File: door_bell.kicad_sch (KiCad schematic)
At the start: 76 parts, among them J1 8-10V AC/DC, J2 Speaker, J3 SWITCH1, J4 SWITCH2, J5 UART, J6 JTAG, J7 BOOT, J8 MicroSD, J9 Door panel, K1 HJR 1-2C, Q1 BC338, SW1 Reset, U1 NCP1117-5v, U2 MAX98357A, U3 NCP1117-3v3, U4 DS3231M, U5 MAX3232, U6 ESP32-WROVER-B, U7 74LVC2G14

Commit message: Update annotations
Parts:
- renumbered D9 to D10, D10 to D11, D11 to D3, D3 to D4, D4 to D5, D5 to D8, D8 to D9, R7 to R10, R10 to R11, R11 to R12, R12 to R13, R13 to R14, R14 to R15, R15 to R16, R16 to R17, R17 to R18, R18 to R19, R19 to R20, R20 to R21, R21 to R22, R22 to R23, R23 to R7

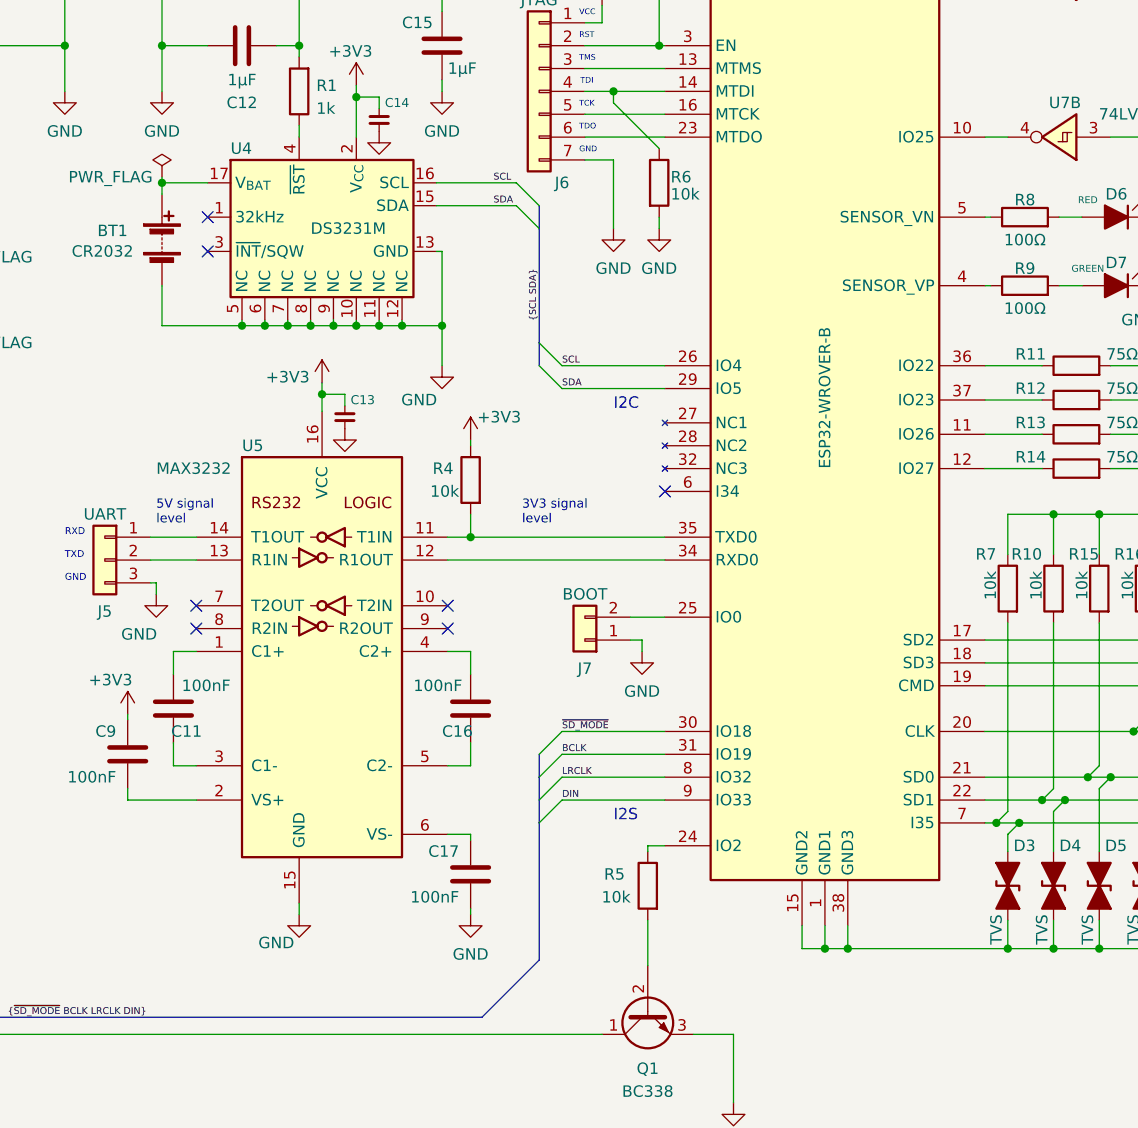
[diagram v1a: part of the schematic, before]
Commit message: Assign footprint for fuse
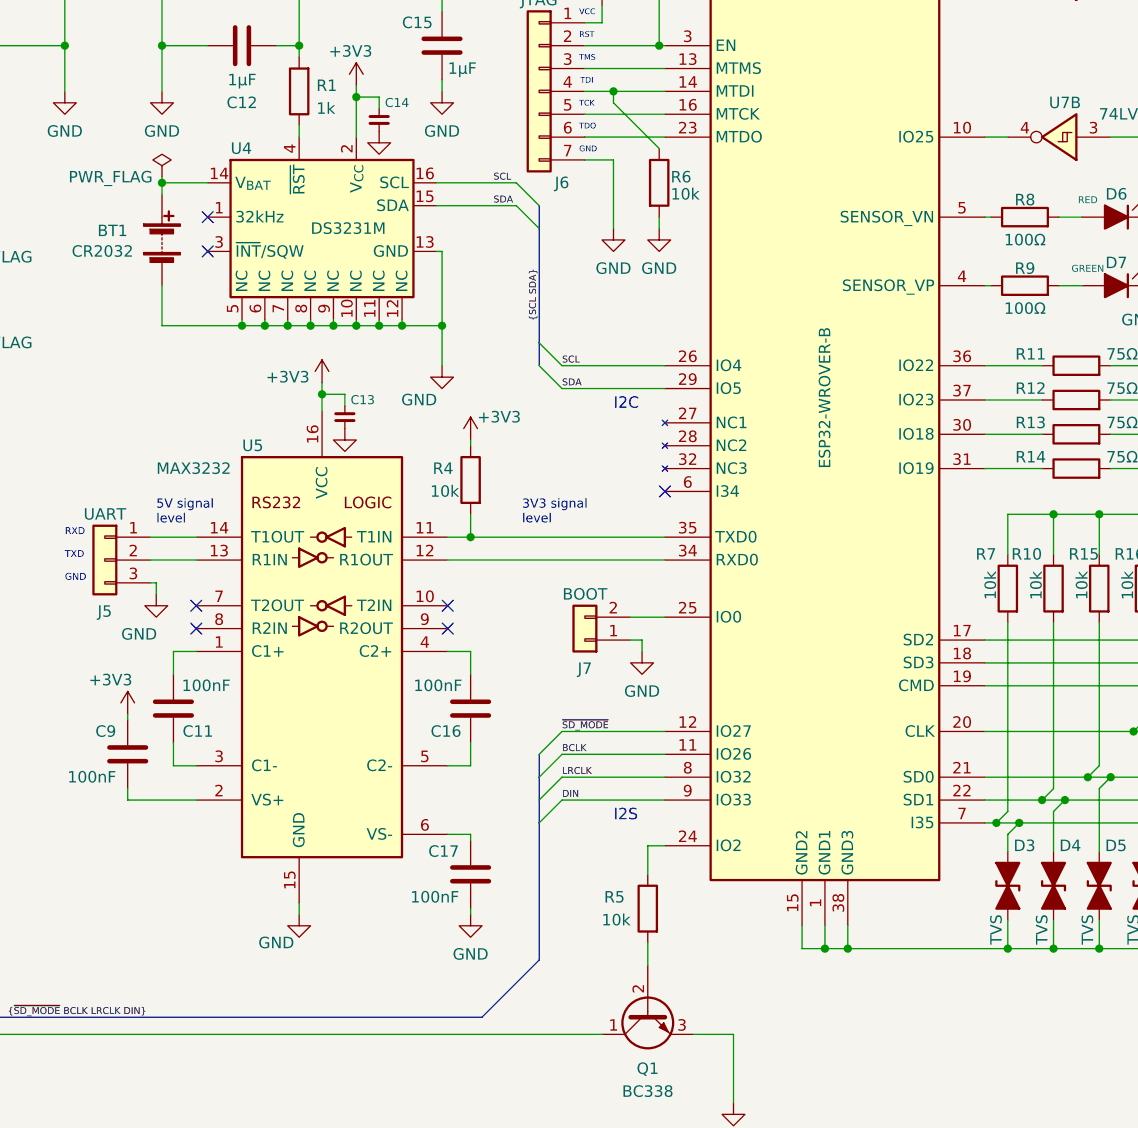
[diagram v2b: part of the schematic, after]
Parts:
- F1: footprint Resistor_SMD:R_0805_2012Metric_Pad1.20x1.40mm_HandSolder -> Fuse_espena:FuseHolder_Keystone_3554
- J1: footprint (none) -> TerminalBlock_Phoenix:TerminalBlock_Phoenix_MKDS-3-2-5.08_1x02_P5.08mm_Horizontal
- J2, SW1: footprint (none) -> TerminalBlock_Phoenix:TerminalBlock_Phoenix_MKDS-1,5-2-5.08_1x02_P5.08mm_Horizontal
- J3, J4: footprint (none) -> TerminalBlock_Phoenix:TerminalBlock_Phoenix_MKDS-1,5-3-5.08_1x03_P5.08mm_Horizontal
- J6: footprint (none) -> Connector_PinHeader_1.27mm:PinHeader_1x07_P1.27mm_Vertical
- J8: footprint (none) -> Connector_Card:microSD_HC_Hirose_DM3AT-SF-PEJM5
- J9: footprint (none) -> TerminalBlock_Phoenix:TerminalBlock_Phoenix_MKDS-1,5-8-5.08_1x08_P5.08mm_Horizontal
- K1: footprint (none) -> Relay_THT_espena:Relay_Tianbo_HJR-1-2C
- U2: footprint Package_DFN_QFN:TQFN-24-1EP_4x4mm_P0.5mm_EP2.6x2.6mm -> Package_DFN_QFN_espena:TQFN-16-1EP_3x3mm_P0.5mm_EP1.23x1.23mm
- U5: footprint Package_SO:TSSOP-16-1EP_4.4x5mm_P0.65mm -> Package_SO_espena:TSSOP-16-1EP_4.4x5mm_P0.65mm
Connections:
- net BCLK: now also U6.11 (IO26); no longer U6.31 (IO19)
- net ~{SD_MODE}: now also U6.12 (IO27); no longer U6.30 (IO18)
- net at BT1.1 (+): now also U4.14 (V_{BAT}); no longer U4.17 (V_{BAT})
- net at R13.1: now also U6.30 (IO18); no longer U6.11 (IO26)
- net at R14.1: now also U6.31 (IO19); no longer U6.12 (IO27)
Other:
- moved on the sheet: R5
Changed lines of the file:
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@@
     (stroke (width 0) (type default))
   )
-  (wire (pts (xy 156.845 139.7) (xy 156.845 140.335))
+  (wire (pts (xy 156.845 139.7) (xy 156.845 142.875))
     (stroke (width 0) (type default))
   )
@@
     (stroke (width 0) (type default))
   )
-  (wire (pts (xy 156.845 147.955) (xy 156.845 153.035))
+  (wire (pts (xy 156.845 150.495) (xy 156.845 153.035))
     (stroke (width 0) (type default))
   )
@@
   (symbol (lib_id "Device:C") (at 104.14 124.46 0) (mirror y) (unit 1)
     (in_bom yes) (on_board yes) (dnp no)
-    (property "Reference" "C11" (at 107.315 127 0)
+    (property "Reference" "C11" (at 108.585 127 0)
       (effects (font (size 1.27 1.27)) (justify left))
     )
@@
       (effects (font (size 1.27 1.27)) (justify left))
     )
-    (property "Footprint" "Package_SO:TSSOP-16-1EP_4.4x5mm_P0.65mm" (at 121.92 140.97 0)
+    (property "Footprint" "Package_SO_espena:TSSOP-16-1EP_4.4x5mm_P0.65mm" (at 121.92 140.97 0)
       (effects (font (size 1.27 1.27)) (justify left) hide)
     )
@@
       (effects (font (size 1.27 1.27)))
     )
-    (property "Footprint" "" (at 24.765 66.04 0)
+    (property "Footprint" "TerminalBlock_Phoenix:TerminalBlock_Phoenix_MKDS-3-2-5.08_1x02_P5.08mm_Horizontal" (at 24.765 66.04 0)
       (effects (font (size 1.27 1.27)) hide)
     )
@@
       (effects (font (size 1.27 1.27)))
     )
-    (property "Footprint" "" (at 309.245 109.22 0)
+    (property "Footprint" "Connector_Card:microSD_HC_Hirose_DM3AT-SF-PEJM5" (at 309.245 109.22 0)
       (effects (font (size 1.27 1.27)) hide)
     )
@@
       (effects (font (size 1.27 1.27)) (justify left))
     )
-    (property "Footprint" "" (at 264.16 48.26 0)
+    (property "Footprint" "TerminalBlock_Phoenix:TerminalBlock_Phoenix_MKDS-1,5-8-5.08_1x08_P5.08mm_Horizontal" (at 264.16 48.26 0)
       (effects (font (size 1.27 1.27)) hide)
     )
@@
       (effects (font (size 1.27 1.27)))
     )
-    (property "Footprint" "" (at 46.99 205.105 0)
+    (property "Footprint" "Relay_THT_espena:Relay_Tianbo_HJR-1-2C" (at 46.99 205.105 0)
       (effects (font (size 1.27 1.27)) hide)
     )
@@
   (symbol (lib_id "Device:C") (at 137.16 124.46 0) (unit 1)
     (in_bom yes) (on_board yes) (dnp no)
-    (property "Reference" "C16" (at 133.985 127 0)
+    (property "Reference" "C16" (at 132.715 127 0)
       (effects (font (size 1.27 1.27)) (justify left))
     )
@@
       (effects (font (size 1.27 1.27)))
     )
-    (property "Footprint" "" (at 111.76 33.655 0)
+    (property "Footprint" "TerminalBlock_Phoenix:TerminalBlock_Phoenix_MKDS-1,5-2-5.08_1x02_P5.08mm_Horizontal" (at 111.76 33.655 0)
       (effects (font (size 1.27 1.27)) hide)
     )
@@
     (pin "12")
     (pin "13")
+    (pin "14")
     (pin "15")
     (pin "16")
-    (pin "17")
     (pin "2")
     (pin "3")
@@
       (effects (font (size 1.27 1.27)))
     )
-    (property "Footprint" "" (at 25.4 182.245 0)
+    (property "Footprint" "TerminalBlock_Phoenix:TerminalBlock_Phoenix_MKDS-1,5-3-5.08_1x03_P5.08mm_Horizontal" (at 25.4 182.245 0)
       (effects (font (size 1.27 1.27)) hide)
     )
@@
       (effects (font (size 1.27 1.27)))
     )
-    (property "Footprint" "" (at 25.4 118.11 0)
+    (property "Footprint" "TerminalBlock_Phoenix:TerminalBlock_Phoenix_MKDS-1,5-2-5.08_1x02_P5.08mm_Horizontal" (at 25.4 118.11 0)
       (effects (font (size 1.27 1.27)) hide)
     )
@@
       (effects (font (size 1.27 1.27)))
     )
-    (property "Footprint" "" (at 144.78 55.88 0)
+    (property "Footprint" "Connector_PinHeader_1.27mm:PinHeader_1x07_P1.27mm_Vertical" (at 144.78 55.88 0)
       (effects (font (size 1.27 1.27)) hide)
     )
@@
       (effects (font (size 1.27 1.27)))
     )
-    (property "Footprint" "Package_DFN_QFN:TQFN-24-1EP_4x4mm_P0.5mm_EP2.6x2.6mm" (at 49.53 161.29 0)
+    (property "Footprint" "Package_DFN_QFN_espena:TQFN-16-1EP_3x3mm_P0.5mm_EP1.23x1.23mm" (at 49.53 161.29 0)
       (effects (font (size 1.27 1.27)) hide)
     )
@@
       (effects (font (size 1.27 1.27)) (justify left))
     )
-    (property "Footprint" "" (at 71.755 182.245 0)
+    (property "Footprint" "TerminalBlock_Phoenix:TerminalBlock_Phoenix_MKDS-1,5-3-5.08_1x03_P5.08mm_Horizontal" (at 71.755 182.245 0)
       (effects (font (size 1.27 1.27)) hide)
     )
@@
     )
   )
-  (symbol (lib_id "Device:R") (at 156.845 144.145 0) (mirror y) (unit 1)
+  (symbol (lib_id "Device:R") (at 156.845 146.685 0) (mirror y) (unit 1)
     (in_bom yes) (on_board yes) (dnp no)
-    (property "Reference" "R5" (at 154.305 142.875 0)
+    (property "Reference" "R5" (at 154.305 145.415 0)
       (effects (font (size 1.27 1.27)) (justify left))
     )
-    (property "Value" "10k" (at 154.94 145.415 0)
+    (property "Value" "10k" (at 154.94 147.955 0)
       (effects (font (size 1.27 1.27)) (justify left))
     )
-    (property "Footprint" "Resistor_SMD:R_0805_2012Metric_Pad1.20x1.40mm_HandSolder" (at 158.623 144.145 90)
+    (property "Footprint" "Resistor_SMD:R_0805_2012Metric_Pad1.20x1.40mm_HandSolder" (at 158.623 146.685 90)
       (effects (font (size 1.27 1.27)) hide)
     )
-    (property "Datasheet" "~" (at 156.845 144.145 0)
+    (property "Datasheet" "~" (at 156.845 146.685 0)
       (effects (font (size 1.27 1.27)) hide)
     )
@@
       (effects (font (size 1.27 1.27)))
     )
-    (property "Footprint" "Resistor_SMD:R_0805_2012Metric_Pad1.20x1.40mm_HandSolder" (at 32.258 73.025 90)
+    (property "Footprint" "Fuse_espena:FuseHolder_Keystone_3554" (at 32.258 73.025 90)
       (effects (font (size 1.27 1.27)) hide)
     )

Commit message: Part placement
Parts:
- removed J4: SWITCH2, TerminalBlock_Phoenix:TerminalBlock_Phoenix_MKDS-1,5-3-5.08_1x03_P5.08mm_Horizontal, symbol Connector:Screw_Terminal_01x03
- BT1: footprint Capacitor_SMD:C_0805_2012Metric_Pad1.18x1.45mm_HandSolder -> Battery:BatteryHolder_Keystone_1058_1x2032
- J1: footprint TerminalBlock_Phoenix:TerminalBlock_Phoenix_MKDS-3-2-5.08_1x02_P5.08mm_Horizontal -> TerminalBlock_Phoenix:TerminalBlock_Phoenix_PT-1,5-2-3.5-H_1x02_P3.50mm_Horizontal
- J2: footprint TerminalBlock_Phoenix:TerminalBlock_Phoenix_MKDS-1,5-2-5.08_1x02_P5.08mm_Horizontal -> TerminalBlock_Phoenix:TerminalBlock_Phoenix_PT-1,5-2-3.5-H_1x02_P3.50mm_Horizontal
- J3: footprint TerminalBlock_Phoenix:TerminalBlock_Phoenix_MKDS-1,5-3-5.08_1x03_P5.08mm_Horizontal -> TerminalBlock_Phoenix:TerminalBlock_Phoenix_PT-1,5-3-3.5-H_1x03_P3.50mm_Horizontal
- J9: footprint TerminalBlock_Phoenix:TerminalBlock_Phoenix_MKDS-1,5-8-5.08_1x08_P5.08mm_Horizontal -> TerminalBlock_Phoenix:TerminalBlock_Phoenix_PT-1,5-8-3.5-H_1x08_P3.50mm_Horizontal
- SW1: footprint TerminalBlock_Phoenix:TerminalBlock_Phoenix_MKDS-1,5-2-5.08_1x02_P5.08mm_Horizontal -> Button_Switch_SMD_espena:SW_SPST_TL3301_6x6mm_H4.3mm
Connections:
- no-connect marks 7 -> 10
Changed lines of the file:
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@@
   (no_connect (at 107.95 73.66))
   (no_connect (at 134.62 113.03))
+  (no_connect (at 55.88 187.325))
   (no_connect (at 106.68 115.57))
   (no_connect (at 107.95 69.85))
+  (no_connect (at 55.88 177.165))
+  (no_connect (at 55.88 182.245))
   (no_connect (at 106.68 113.03))
   (no_connect (at 134.62 115.57))
@@
     (stroke (width 0) (type default))
   )
-  (wire (pts (xy 55.88 177.165) (xy 59.69 177.165))
-    (stroke (width 0) (type default))
-  )
   (wire (pts (xy 149.86 58.42) (xy 158.75 58.42))
     (stroke (width 0) (type default))
@@
     (stroke (width 0) (type default))
   )
-  (wire (pts (xy 59.69 184.785) (xy 66.675 184.785))
-    (stroke (width 0) (type default))
-  )
   (wire (pts (xy 243.84 45.72) (xy 243.84 60.96))
     (stroke (width 0) (type default))
@@
     (stroke (width 0) (type default))
   )
-  (wire (pts (xy 59.69 184.785) (xy 59.69 187.325))
-    (stroke (width 0) (type default))
-  )
   (wire (pts (xy 234.95 22.86) (xy 234.95 34.29))
     (stroke (width 0) (type default))
@@
     (stroke (width 0) (type default))
   )
-  (wire (pts (xy 55.88 182.245) (xy 66.675 182.245))
-    (stroke (width 0) (type default))
-  )
   (wire (pts (xy 43.18 36.195) (xy 43.18 50.8))
     (stroke (width 0) (type default))
@@
     (stroke (width 0) (type default))
   )
-  (wire (pts (xy 59.69 179.705) (xy 66.675 179.705))
-    (stroke (width 0) (type default))
-  )
   (wire (pts (xy 30.48 182.245) (xy 40.64 182.245))
     (stroke (width 0) (type default))
@@
     (stroke (width 0) (type default))
   )
-  (wire (pts (xy 59.69 177.165) (xy 59.69 179.705))
-    (stroke (width 0) (type default))
-  )
   (bus (pts (xy 222.25 95.25) (xy 222.25 91.44))
     (stroke (width 0) (type default))
   )
-  (wire (pts (xy 55.88 187.325) (xy 59.69 187.325))
-    (stroke (width 0) (type default))
-  )
   (wire (pts (xy 48.26 142.24) (xy 48.26 144.78))
     (stroke (width 0) (type default))
@@
     (effects (font (size 0.635 0.635)) (justify left bottom))
   )
-  (text "NC" (at 74.295 182.88 0)
-    (effects (font (size 1.27 1.27)) (justify left bottom))
-  )
   (text "RXD" (at 92.075 105.41 0)
     (effects (font (size 0.762 0.762)) (justify left bottom))
@@
     (effects (font (size 1.016 1.016)) (justify left bottom))
   )
-  (text "COM" (at 74.295 180.34 0)
-    (effects (font (size 1.27 1.27)) (justify left bottom))
-  )
   (text "NC" (at 20.32 182.88 0)
     (effects (font (size 1.27 1.27)) (justify left bottom))
@@
     (effects (font (size 1.27 1.27)) (justify left bottom))
   )
-  (text "NO" (at 74.295 185.42 0)
-    (effects (font (size 1.27 1.27)) (justify left bottom))
-  )
   (text "TDO" (at 149.225 60.325 0)
     (effects (font (size 0.635 0.635)) (justify left bottom))
@@
       (effects (font (size 1.27 1.27)) (justify right))
     )
-    (property "Footprint" "Capacitor_SMD:C_0805_2012Metric_Pad1.18x1.45mm_HandSolder" (at 102.87 70.866 90)
+    (property "Footprint" "Battery:BatteryHolder_Keystone_1058_1x2032" (at 102.87 70.866 90)
       (effects (font (size 1.27 1.27)) hide)
     )
@@
       (effects (font (size 1.27 1.27)))
     )
-    (property "Footprint" "TerminalBlock_Phoenix:TerminalBlock_Phoenix_MKDS-3-2-5.08_1x02_P5.08mm_Horizontal" (at 24.765 66.04 0)
+    (property "Footprint" "TerminalBlock_Phoenix:TerminalBlock_Phoenix_PT-1,5-2-3.5-H_1x02_P3.50mm_Horizontal" (at 24.765 66.04 0)
       (effects (font (size 1.27 1.27)) hide)
     )
@@
       (effects (font (size 1.27 1.27)) (justify left))
     )
-    (property "Footprint" "TerminalBlock_Phoenix:TerminalBlock_Phoenix_MKDS-1,5-8-5.08_1x08_P5.08mm_Horizontal" (at 264.16 48.26 0)
+    (property "Footprint" "TerminalBlock_Phoenix:TerminalBlock_Phoenix_PT-1,5-8-3.5-H_1x08_P3.50mm_Horizontal" (at 264.16 48.26 0)
       (effects (font (size 1.27 1.27)) hide)
     )
@@
       (effects (font (size 1.27 1.27)))
     )
-    (property "Footprint" "TerminalBlock_Phoenix:TerminalBlock_Phoenix_MKDS-1,5-2-5.08_1x02_P5.08mm_Horizontal" (at 111.76 33.655 0)
+    (property "Footprint" "Button_Switch_SMD_espena:SW_SPST_TL3301_6x6mm_H4.3mm" (at 111.76 33.655 0)
       (effects (font (size 1.27 1.27)) hide)
     )
@@
       (effects (font (size 1.27 1.27)))
     )
-    (property "Footprint" "TerminalBlock_Phoenix:TerminalBlock_Phoenix_MKDS-1,5-3-5.08_1x03_P5.08mm_Horizontal" (at 25.4 182.245 0)
+    (property "Footprint" "TerminalBlock_Phoenix:TerminalBlock_Phoenix_PT-1,5-3-3.5-H_1x03_P3.50mm_Horizontal" (at 25.4 182.245 0)
       (effects (font (size 1.27 1.27)) hide)
     )
@@
       (effects (font (size 1.27 1.27)))
     )
-    (property "Footprint" "TerminalBlock_Phoenix:TerminalBlock_Phoenix_MKDS-1,5-2-5.08_1x02_P5.08mm_Horizontal" (at 25.4 118.11 0)
+    (property "Footprint" "TerminalBlock_Phoenix:TerminalBlock_Phoenix_PT-1,5-2-3.5-H_1x02_P3.50mm_Horizontal" (at 25.4 118.11 0)
       (effects (font (size 1.27 1.27)) hide)
     )
@@
         )
       )
-    )
-  )
-  (symbol (lib_id "Connector:Screw_Terminal_01x03") (at 71.755 182.245 0) (unit 1)
-    (in_bom yes) (on_board yes) (dnp no)
-    (property "Reference" "J4" (at 70.485 173.99 0)
-      (effects (font (size 1.27 1.27)) (justify left))
-    )
-    (property "Value" "SWITCH2" (at 67.945 176.53 0)
-      (effects (font (size 1.27 1.27)) (justify left))
-    )
-    (property "Footprint" "TerminalBlock_Phoenix:TerminalBlock_Phoenix_MKDS-1,5-3-5.08_1x03_P5.08mm_Horizontal" (at 71.755 182.245 0)
-      (effects (font (size 1.27 1.27)) hide)
-    )
-    (property "Datasheet" "~" (at 71.755 182.245 0)
-      (effects (font (size 1.27 1.27)) hide)
-    )
-    (pin "1")
-    (pin "2")
-    (pin "3")
-    (instances
-      (project "door_bell"
-        (path "/c78ad4c4-54c1-4b1d-a971-e4b8abed6bf8"
-          (reference "J4") (unit 1)
-        )
-      )

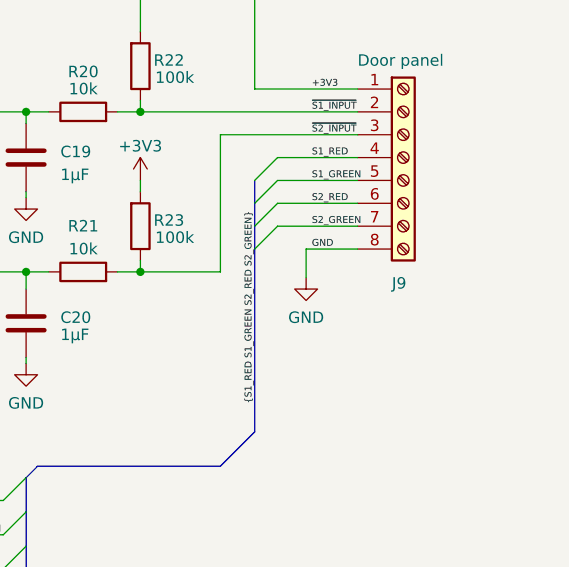
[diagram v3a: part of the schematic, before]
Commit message: Part placement and silk screen adjustments
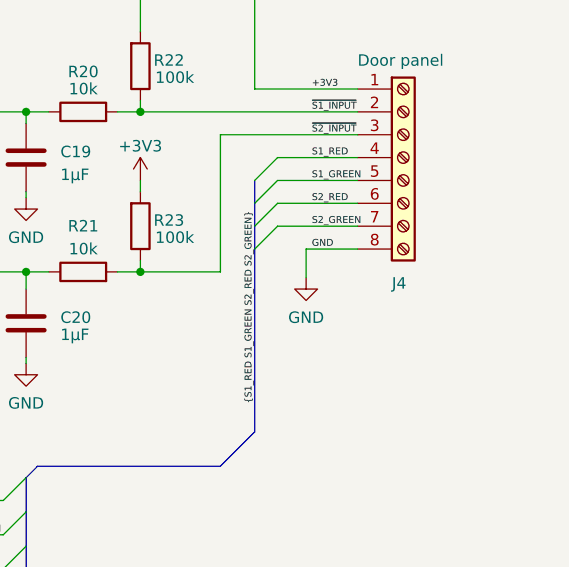
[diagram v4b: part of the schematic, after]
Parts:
- renumbered J9 to J4
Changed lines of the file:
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@@
   (symbol (lib_id "Connector:Screw_Terminal_01x08") (at 264.16 48.26 0) (unit 1)
     (in_bom yes) (on_board yes) (dnp no)
-    (property "Reference" "J9" (at 262.89 62.23 0)
+    (property "Reference" "J4" (at 262.89 62.23 0)
       (effects (font (size 1.27 1.27)) (justify left))
     )
@@
       (project "door_bell"
         (path "/c78ad4c4-54c1-4b1d-a971-e4b8abed6bf8"
-          (reference "J9") (unit 1)
+          (reference "J4") (unit 1)
         )
       )
